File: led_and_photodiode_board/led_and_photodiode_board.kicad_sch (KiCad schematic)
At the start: 45 parts, among them J1 Conn_01x02_Socket, J2 DS1013-01-10RSiB-B, U1 ULN2803A (SOIC-18)

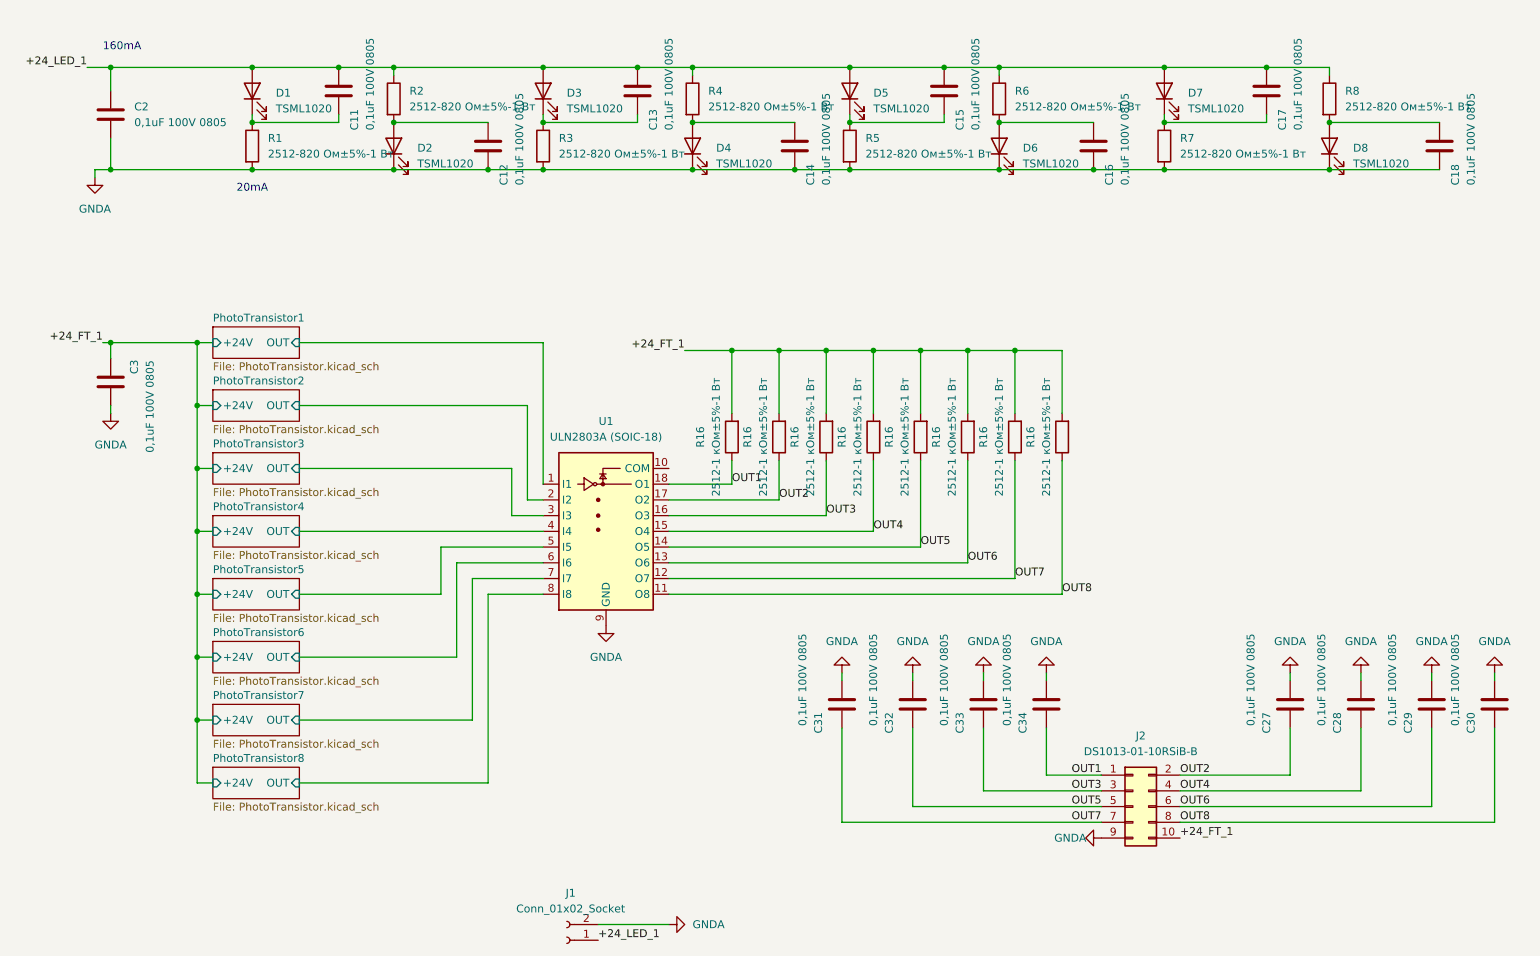
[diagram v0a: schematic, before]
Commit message: led_and_photo замена цепь формирования выходного сигнала
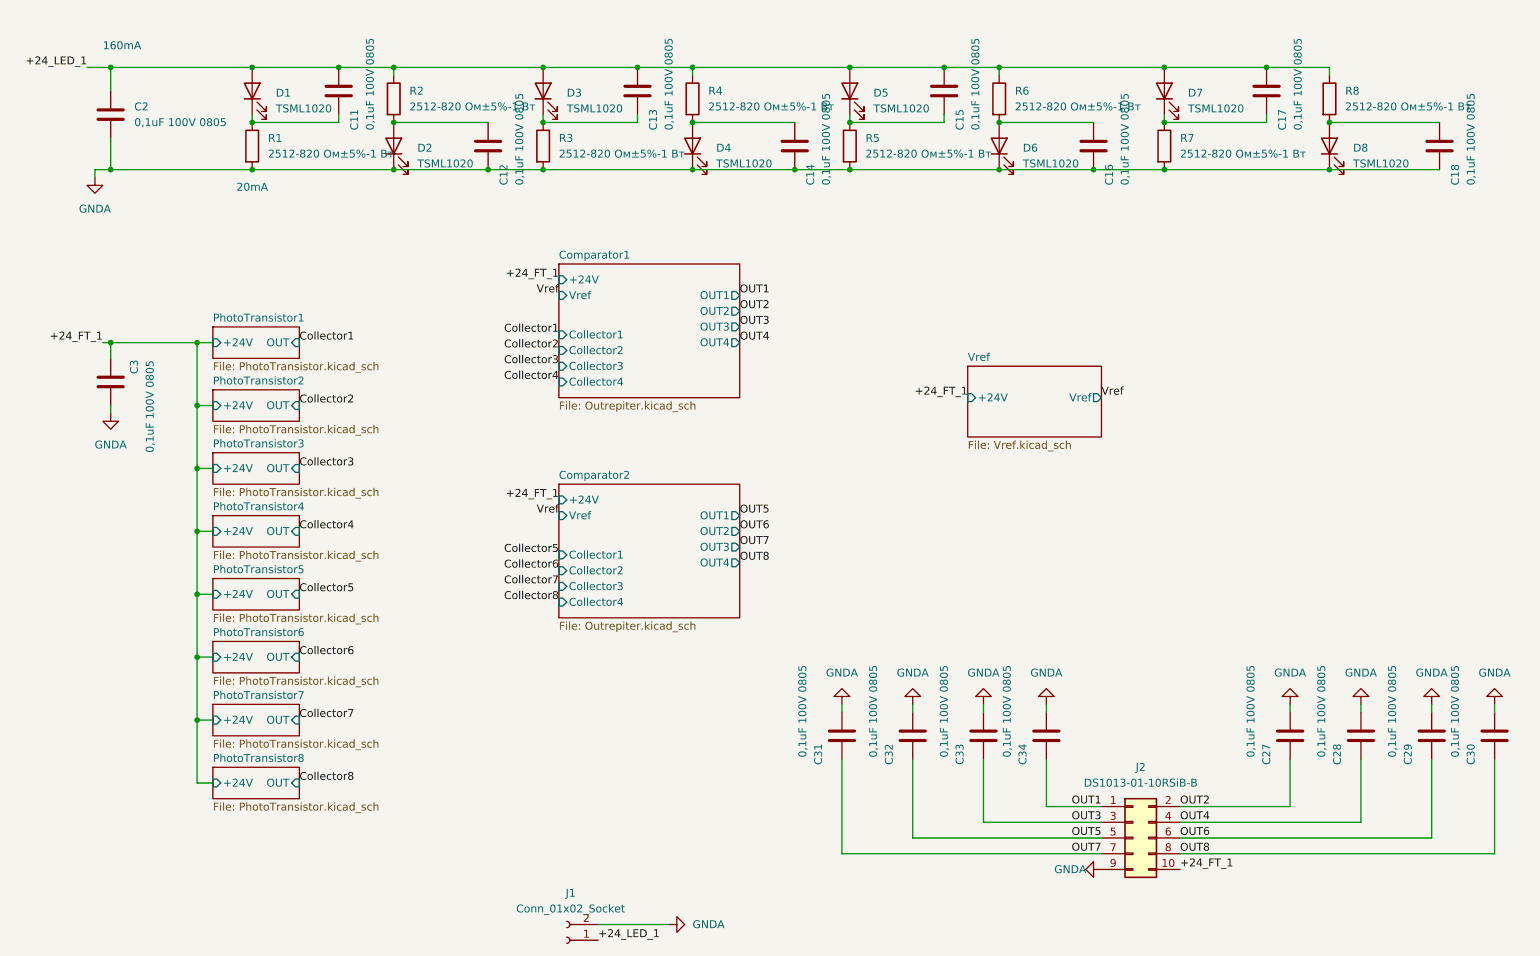
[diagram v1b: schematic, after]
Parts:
- removed R16 (x8): 2512-1 кОм±5%-1 Вт, PCM_Resistor_SMD_AKL:R_2512_6332Metric_Pad1.52x3.35mm_HandSolder, symbol Device:R
- removed U1: ULN2803A (SOIC-18), Package_SO:SOIC-18W_7.5x11.6mm_P1.27mm, symbol Transistor_Array:ULN2803A
- J1: footprint Connector:PAD_3x3mm_02 -> Connector:PAD_5x5_02
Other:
- added sheet Comparator1 (Outrepiter.kicad_sch)
- added sheet Comparator2 (Outrepiter.kicad_sch)
- added sheet Vref (Vref.kicad_sch)
- moved on the sheet: C27, C28, C29, C30, C31, C32, C33, C34, J2

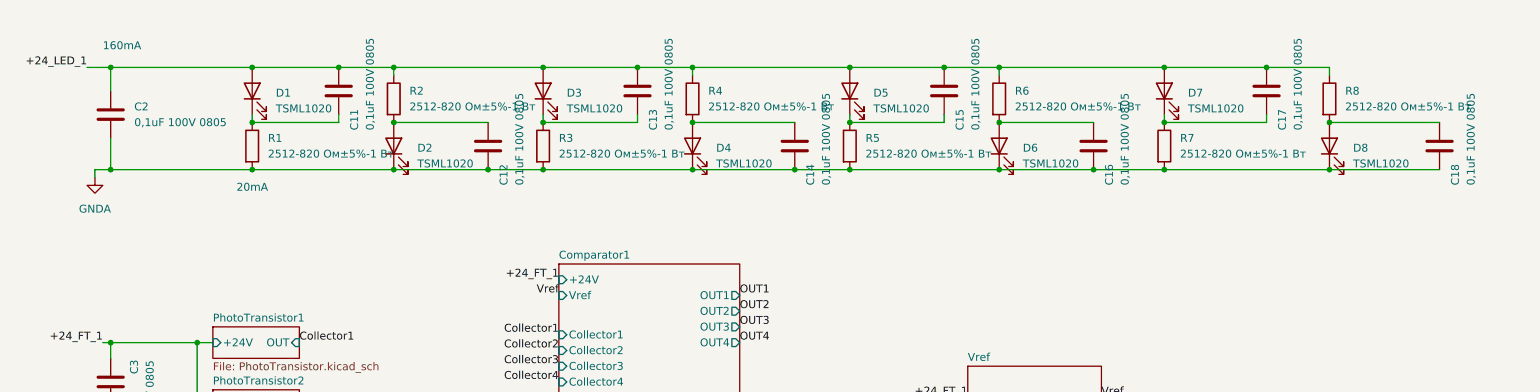
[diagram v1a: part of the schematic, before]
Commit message: ledphoto коррекция схемы
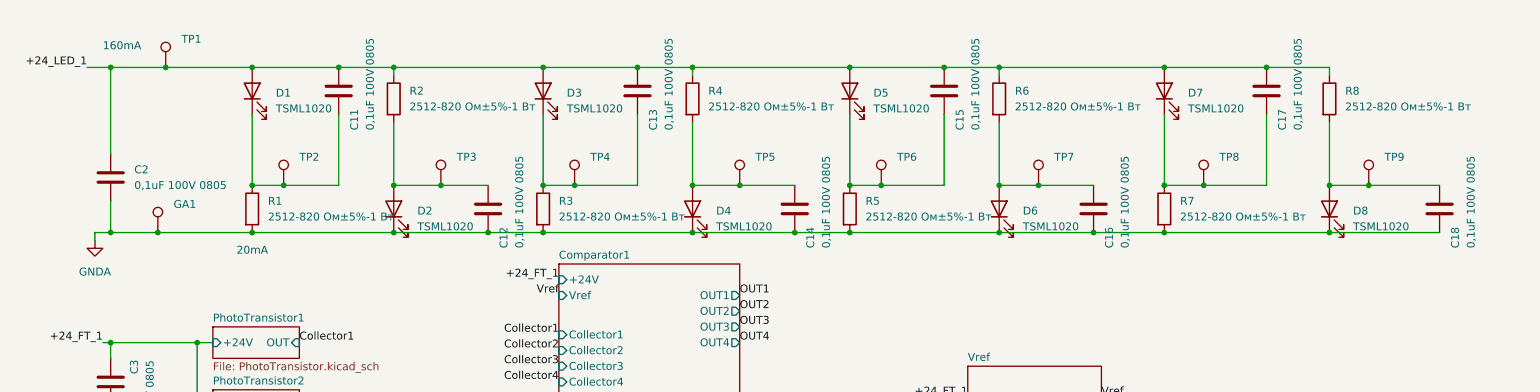
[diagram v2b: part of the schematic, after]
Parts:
- added GA1, TP1, TP2, TP3, TP4, TP5, TP6, TP7, TP8, TP9: TestPoint, TestPoint:TestPoint_Pad_D1.0mm, symbol Connector:TestPoint
- C11, C12, C13, C14, C15, C16, C17, C18, C2, C27, C28, C29, C3, C30, C31, C32, C33, C34: footprint PCM_Resistor_SMD_AKL:R_0805_2012Metric_Pad1.20x1.40mm_HandSolder -> Capacitor_SMD:C_0805_2012Metric
- D1, D2, D3, D4, D5, D6, D7, D8: footprint PCM_Diode_SMD_Handsoldering_AKL:D_MiniMELF -> Diode_SMD:D_MiniMELF
- R1, R2, R3, R4, R5, R6, R7, R8: footprint PCM_Resistor_SMD_AKL:R_2512_6332Metric_Pad1.40x3.35mm_HandSolder -> Resistor_SMD:R_2512_6332Metric
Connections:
- net +24_LED_1: now also TP1.1
- net GNDA: now also GA1.1
- net at C18.1, D8.2 (A), R8.2: now also TP9.1
- net at C16.1, D6.2 (A), R6.2: now also TP7.1
- net at C17.2, D7.1 (K), R7.1: now also TP8.1
- net at C13.2, D3.1 (K), R3.1: now also TP4.1
- net at C12.1, D2.2 (A), R2.2: now also TP3.1
- net at C14.1, D4.2 (A), R4.2: now also TP5.1
- net at C11.2, D1.1 (K), R1.1: now also TP2.1
- net at C15.2, D5.1 (K), R5.1: now also TP6.1
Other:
- moved on the sheet: C12, C14, C16, C18, C2, D2, D4, D6, D8, R1, R3, R5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

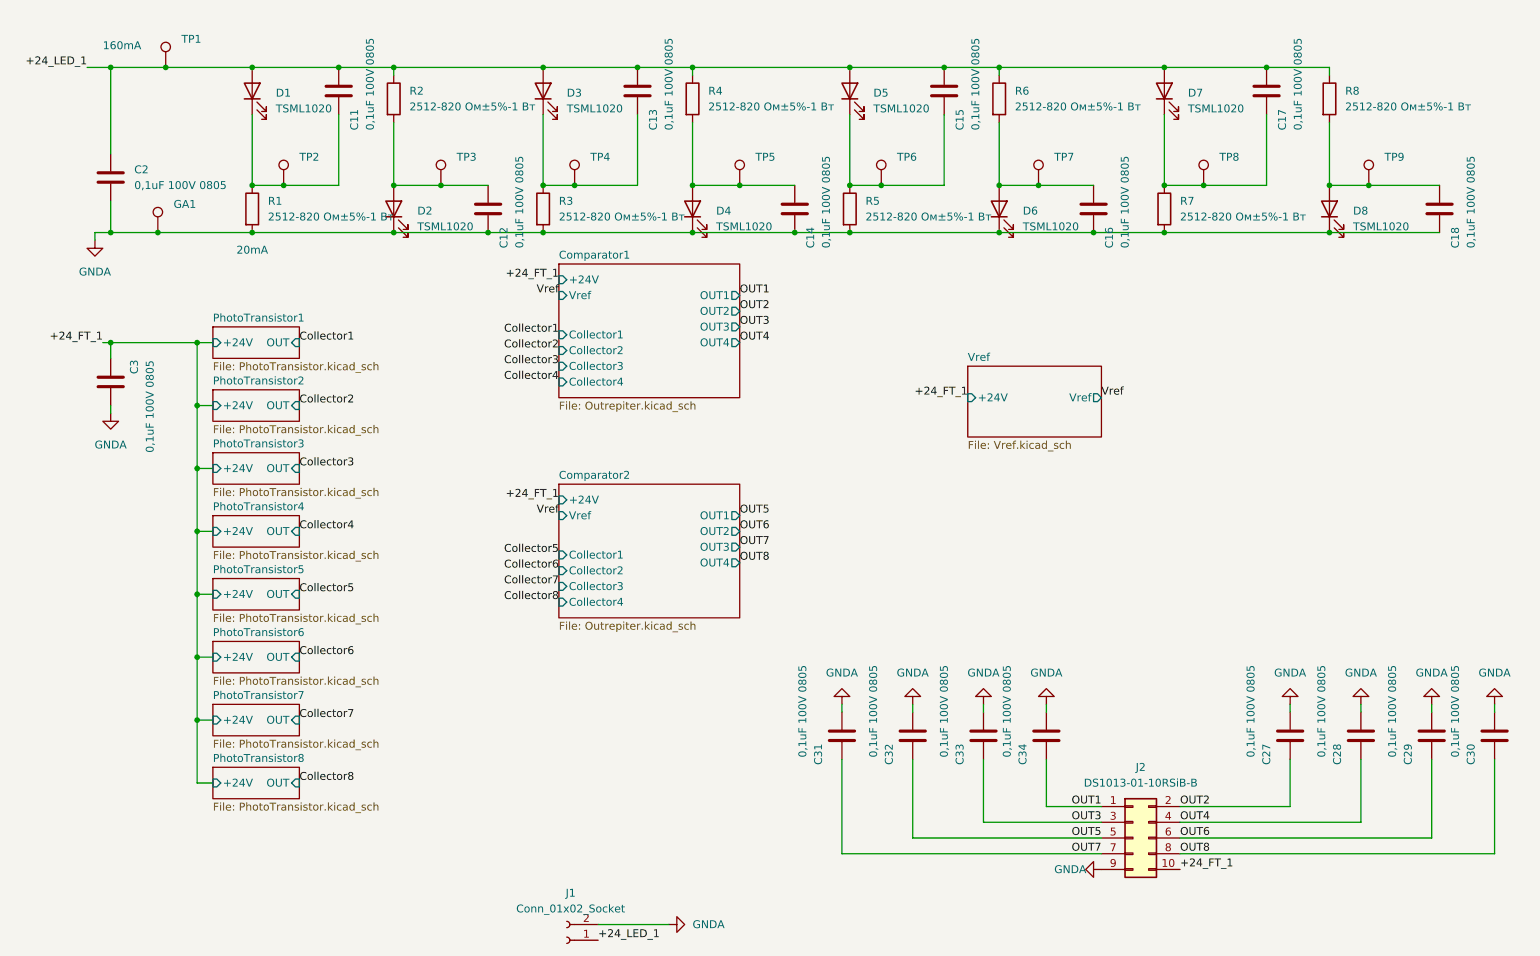
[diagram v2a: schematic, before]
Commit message: ledphoto обновление питания светодиодов
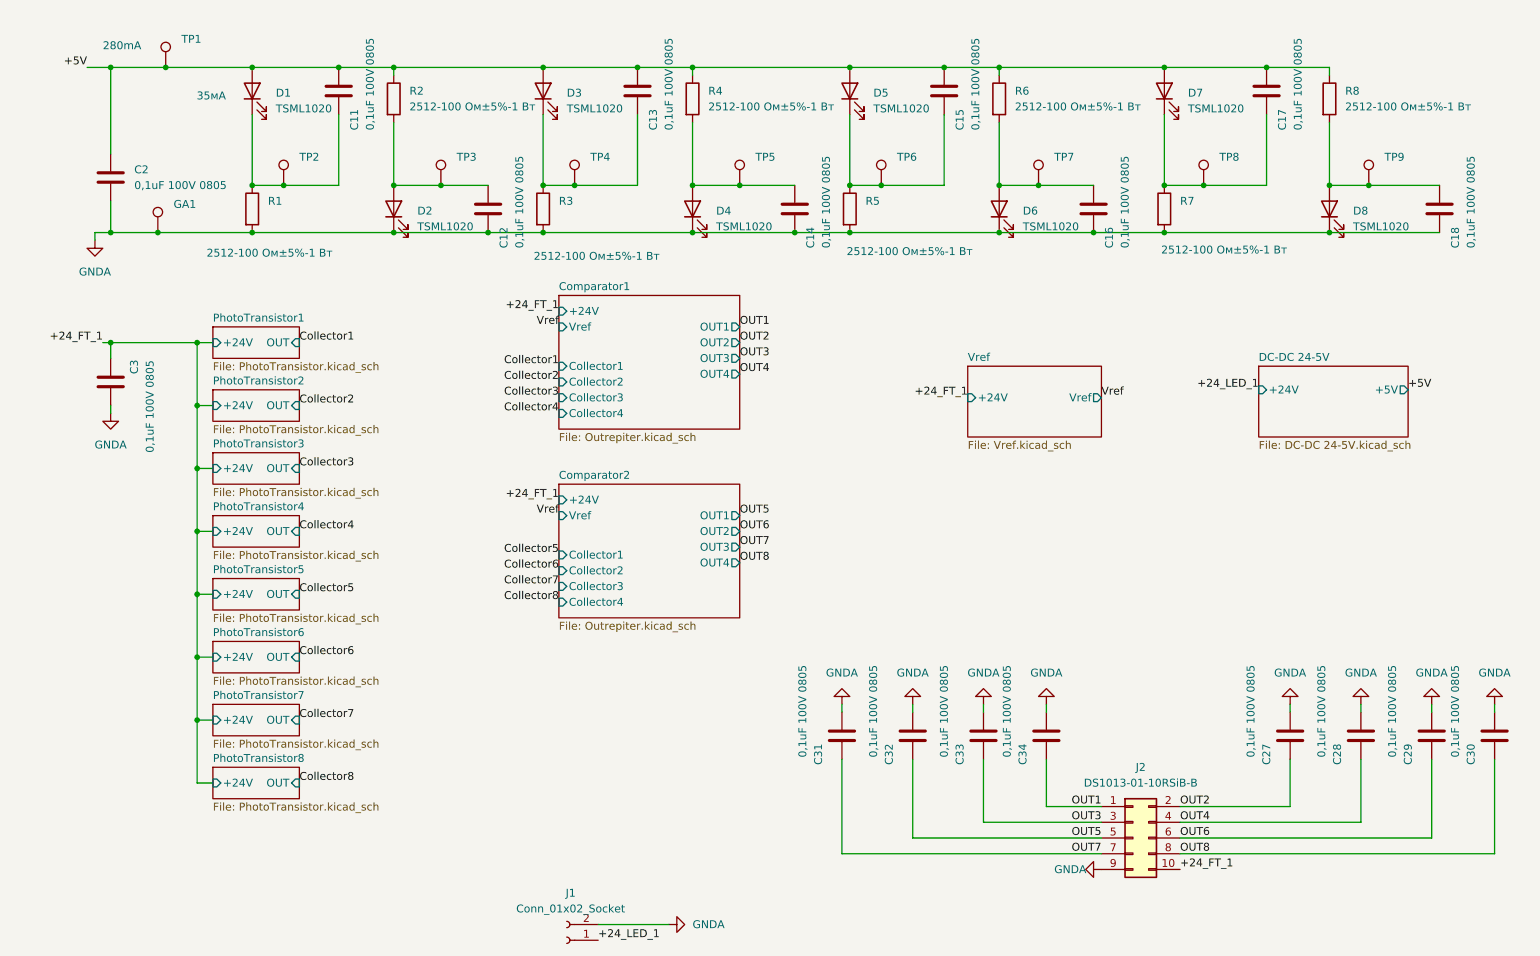
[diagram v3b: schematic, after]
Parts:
- R1, R2, R3, R4, R5, R6, R7, R8: value 2512-820 Ом±5%-1 Вт -> 2512-100 Ом±5%-1 Вт
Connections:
- net +24_LED_1: no longer C11.1, C13.1, C15.1, C17.1, C2.1, D1.2 (A), D3.2 (A), D5.2 (A), D7.2 (A), R2.1, R4.1, R6.1, R8.1, TP1.1
- new net +5V: C11.1, C13.1, C15.1, C17.1, C2.1, D1.2 (A), D3.2 (A), D5.2 (A), D7.2 (A), R2.1, R4.1, R6.1, R8.1, TP1.1
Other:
- added sheet DC-DC 24-5V (DC-DC 24-5V.kicad_sch)
- note added: "280mA"
- note added: "35мА"
- note removed: "160mA"
- note removed: "20mA"
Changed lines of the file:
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@@
 		)
 	)
-	(text "20mA"
+	(text "35мА"
 		(exclude_from_sim no)
-		(at 62.23 58.42 0)
+		(at 58.166 32.766 0)
 		(effects
 			(font
 				(size 1.27 1.27)
 			)
-			(justify left bottom)
 		)
 	)
-	(text "160mA"
+	(text "280mA"
 		(exclude_from_sim no)
 		(at 40.64 25.4 0)
@@
 	)
 	(label "Vref"
-		(at 114.3 64.77 180)
+		(at 114.3 69.85 180)
 		(fields_autoplaced yes)
 		(effects
@@
 	)
 	(label "OUT3"
-		(at 143.51 69.85 0)
+		(at 143.51 74.93 0)
 		(fields_autoplaced yes)
 		(effects
@@
 	)
 	(label "Collector4"
-		(at 114.3 78.74 180)
+		(at 114.3 83.82 180)
 		(fields_autoplaced yes)
 		(effects
@@
 	)
 	(label "OUT4"
-		(at 143.51 72.39 0)
+		(at 143.51 77.47 0)
 		(fields_autoplaced yes)
 		(effects
@@
 	)
 	(label "OUT2"
-		(at 143.51 67.31 0)
+		(at 143.51 72.39 0)
 		(fields_autoplaced yes)
 		(effects
@@
 	)
 	(label "Collector2"
-		(at 114.3 73.66 180)
+		(at 114.3 78.74 180)
 		(fields_autoplaced yes)
 		(effects
@@
 	)
 	(label "Collector3"
-		(at 114.3 76.2 180)
+		(at 114.3 81.28 180)
 		(fields_autoplaced yes)
 		(effects
@@
 	)
 	(label "OUT1"
-		(at 143.51 64.77 0)
+		(at 143.51 69.85 0)
 		(fields_autoplaced yes)
 		(effects
@@
 	)
 	(label "+24_FT_1"
-		(at 114.3 62.23 180)
+		(at 114.3 67.31 180)
 		(fields_autoplaced yes)
 		(effects
@@
 		)
 	)
+	(label "+5V"
+		(at 38.1 27.94 180)
+		(fields_autoplaced yes)
+		(effects
+			(font
+				(size 1.27 1.27)
+			)
+			(justify right bottom)
+		)
+	)
 	(label "OUT1"
 		(at 201.93 147.32 180)
@@
 		)
 	)
+	(label "+5V"
+		(at 251.46 80.01 0)
+		(fields_autoplaced yes)
+		(effects
+			(font
+				(size 1.27 1.27)
+			)
+			(justify left bottom)
+		)
+	)
 	(label "+24_FT_1"
 		(at 180.34 81.28 180)
@@
 		)
 	)
-	(label "Collector1"
-		(at 114.3 71.12 180)
+	(label "+24_LED_1"
+		(at 227.33 80.01 180)
 		(fields_autoplaced yes)
 		(effects
@@
 		)
 	)
-	(label "+24_LED_1"
-		(at 38.1 27.94 180)
+	(label "Collector1"
+		(at 114.3 76.2 180)
 		(fields_autoplaced yes)
 		(effects
@@
 			)
 		)
-		(property "Value" "2512-820 Ом±5%-1 Вт"
+		(property "Value" "2512-100 Ом±5%-1 Вт"
 			(at 241.3 34.29 0)
 			(effects
@@
 		(on_board yes)
 		(dnp no)
-		(fields_autoplaced yes)
 		(property "Reference" "R7"
 			(at 214.63 49.53 0)
@@
 			)
 		)
-		(property "Value" "2512-820 Ом±5%-1 Вт"
-			(at 214.63 52.07 0)
+		(property "Value" "2512-100 Ом±5%-1 Вт"
+			(at 211.582 57.404 0)
 			(effects
 				(font
@@
 		(on_board yes)
 		(dnp no)
-		(fields_autoplaced yes)
 		(property "Reference" "R3"
 			(at 114.3 49.53 0)
@@
 			)
 		)
-		(property "Value" "2512-820 Ом±5%-1 Вт"
-			(at 114.3 52.07 0)
+		(property "Value" "2512-100 Ом±5%-1 Вт"
+			(at 110.236 58.42 0)
 			(effects
 				(font
@@
 			)
 		)
-		(property "Value" "2512-820 Ом±5%-1 Вт"
+		(property "Value" "2512-100 Ом±5%-1 Вт"
 			(at 138.43 34.29 0)
 			(effects
@@
 		(on_board yes)
 		(dnp no)
-		(fields_autoplaced yes)
 		(property "Reference" "R1"
 			(at 67.31 49.53 0)
@@
 			)
 		)
-		(property "Value" "2512-820 Ом±5%-1 Вт"
-			(at 67.31 52.07 0)
+		(property "Value" "2512-100 Ом±5%-1 Вт"
+			(at 57.404 57.912 0)
 			(effects
 				(font
@@
 			)
 		)
-		(property "Value" "2512-820 Ом±5%-1 Вт"
+		(property "Value" "2512-100 Ом±5%-1 Вт"
 			(at 187.96 34.29 0)
 			(effects
@@
 			)
 		)
-		(property "Value" "2512-820 Ом±5%-1 Вт"
+		(property "Value" "2512-100 Ом±5%-1 Вт"
 			(at 90.17 34.29 0)
 			(effects
@@
 		(on_board yes)
 		(dnp no)
-		(fields_autoplaced yes)
 		(property "Reference" "R5"
 			(at 163.83 49.53 0)
@@
 			)
 		)
-		(property "Value" "2512-820 Ом±5%-1 Вт"
-			(at 163.83 52.07 0)
+		(property "Value" "2512-100 Ом±5%-1 Вт"
+			(at 160.782 57.658 0)
 			(effects
 				(font
@@
 	)
 	(sheet
-		(at 114.3 59.69)
+		(at 114.3 64.77)
 		(size 29.21 21.59)
 		(fields_autoplaced yes)
@@
 		)
 		(property "Sheetname" "Comparator1"
-			(at 114.3 58.9784 0)
+			(at 114.3 64.0584 0)
 			(effects
 				(font
@@
 		)
 		(property "Sheetfile" "Outrepiter.kicad_sch"
-			(at 114.3 81.8646 0)
+			(at 114.3 86.9446 0)
 			(effects
 				(font
@@
 		)
 		(pin "+24V" input
-			(at 114.3 62.23 180)
+			(at 114.3 67.31 180)
 			(effects
 				(font
@@
 		)
 		(pin "OUT1" output
-			(at 143.51 64.77 0)
+			(at 143.51 69.85 0)
 			(effects
 				(font
@@
 		)
 		(pin "OUT2" output
-			(at 143.51 67.31 0)
+			(at 143.51 72.39 0)
 			(effects
 				(font
@@
 		)
 		(pin "Vref" input
-			(at 114.3 64.77 180)
+			(at 114.3 69.85 180)
 			(effects
 				(font
@@
 		)
 		(pin "Collector4" input
-			(at 114.3 78.74 180)
+			(at 114.3 83.82 180)
 			(effects
 				(font
@@
 		)
 		(pin "Collector1" input
-			(at 114.3 71.12 180)
+			(at 114.3 76.2 180)
 			(effects
 				(font
@@
 		)
 		(pin "Collector3" input
-			(at 114.3 76.2 180)
+			(at 114.3 81.28 180)
 			(effects
 				(font
@@
 		)
 		(pin "Collector2" input
-			(at 114.3 73.66 180)
+			(at 114.3 78.74 180)
 			(effects
 				(font
@@
 		)
 		(pin "OUT3" output
-			(at 143.51 69.85 0)
+			(at 143.51 74.93 0)
 			(effects
 				(font
@@
 		)
 		(pin "OUT4" output
-			(at 143.51 72.39 0)
+			(at 143.51 77.47 0)
 			(effects
 				(font
@@
 				)
 			)
+		)
+	)
+	(sheet
+		(at 227.33 76.2)
+		(size 24.13 11.43)
+		(fields_autoplaced yes)
+		(stroke
+			(width 0.1524)
+			(type solid)
+		)
+		(fill
+			(color 0 0 0 0.0000)
+		)
+		(property "Sheetname" "DC-DC 24-5V"
+			(at 227.33 75.4884 0)
+			(effects
+				(font
+					(size 1.27 1.27)
+				)
+				(justify left bottom)
+			)
+		)
+		(property "Sheetfile" "DC-DC 24-5V.kicad_sch"
+			(at 227.33 88.2146 0)
+			(effects
+				(font
+					(size 1.27 1.27)
+				)
+				(justify left top)
+			)
+		)
+		(pin "+5V" output
+			(at 251.46 80.01 0)
+			(effects
+				(font
+					(size 1.27 1.27)
+				)
+				(justify right)
+			)
+		)
+		(pin "+24V" input
+			(at 227.33 80.01 180)
+			(effects
+				(font
+					(size 1.27 1.27)
+				)
+				(justify left)
+			)
+		)
+		(instances
+			(project "led_and_photodiode_board"
+				(path "/f4cecc67-0bcd-4036-b070-4b6cf1ef2c64"
+					(page "13")
+				)
+			)
